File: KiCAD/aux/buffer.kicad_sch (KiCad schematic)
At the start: 9 parts, among them J3 Conn_Coaxial_Small, T1 WB1-1L, U2 AD8055ARTZ-R2

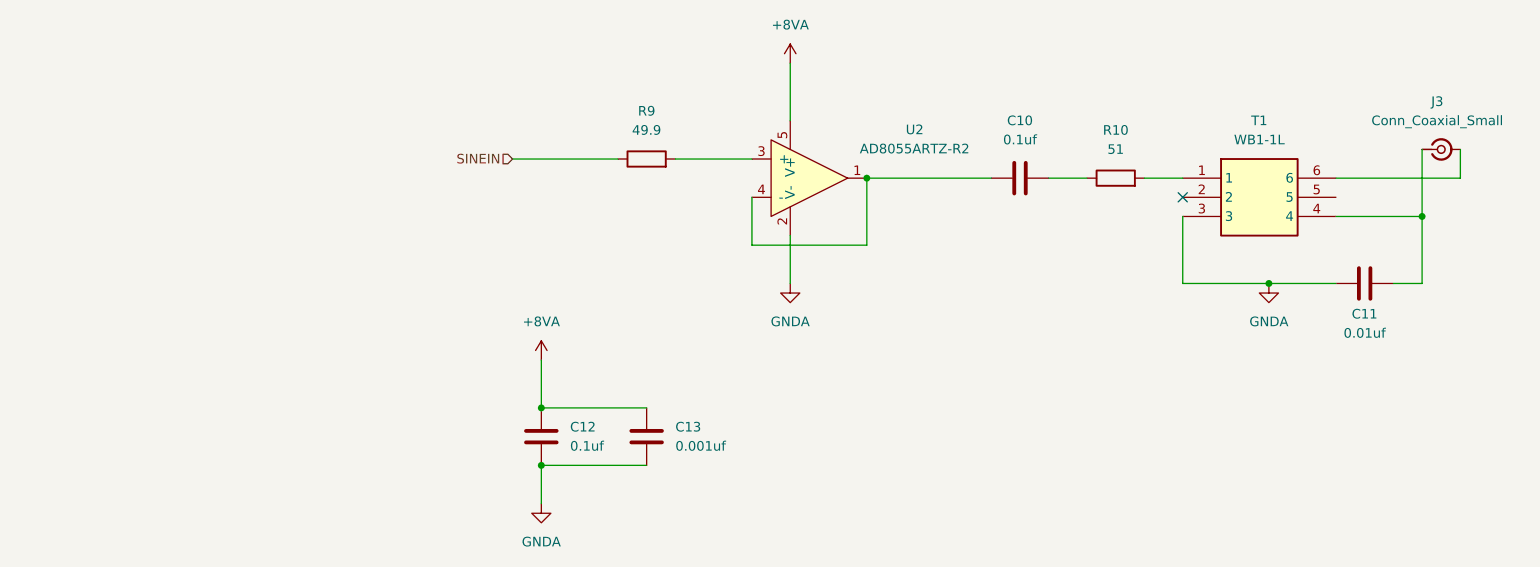
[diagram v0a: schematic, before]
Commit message: Reworked, now with IRIG option board complete
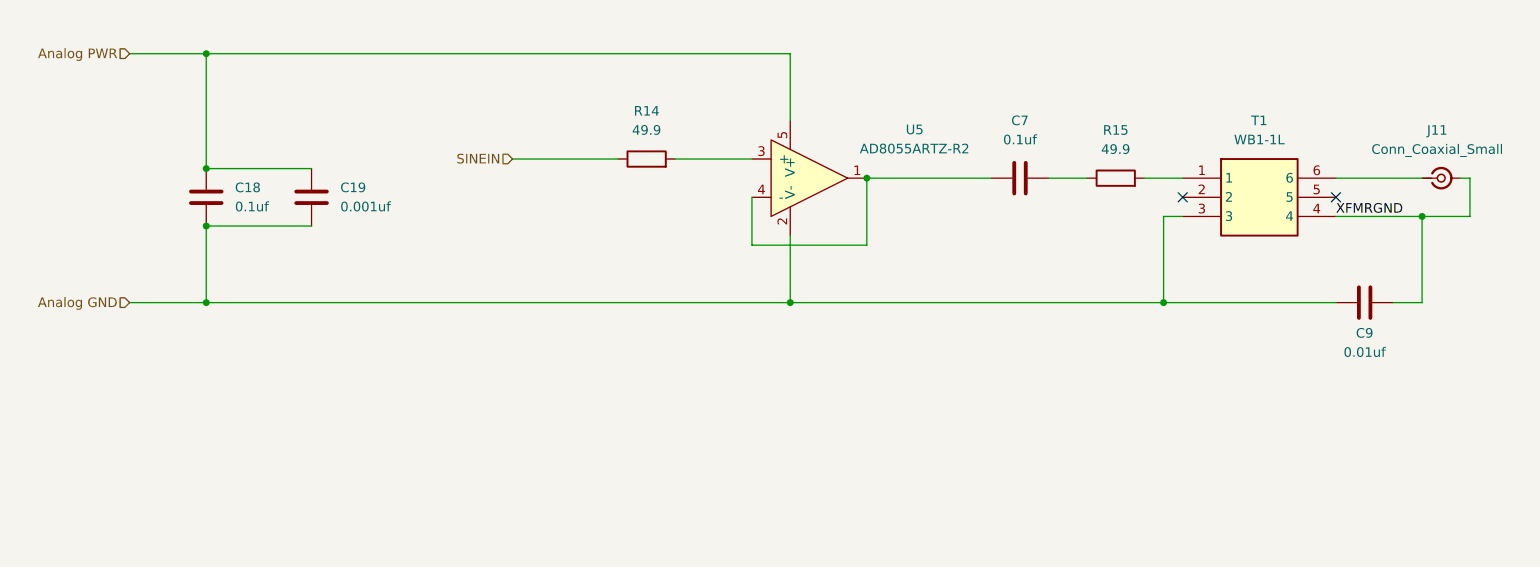
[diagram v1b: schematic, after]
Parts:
- R15: renamed from R10; value 51 -> 49.9
- renumbered C12 to C18, C13 to C19, C10 to C7, C11 to C9, J3 to J11, R9 to R14, U2 to U5
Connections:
- net XFMRGND: now reaches C9.2, T1.4
- net XFMRGND: now also J11.2 (Ext); no longer J11.1 (In)
- net at T1.6: now also J11.1 (In); no longer J11.2 (Ext)
- net +8VA renamed Analog PWR
- net GNDA renamed Analog GND
- no-connect marks 1 -> 2
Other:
- moved on the sheet: C18, C19, C9, J11
